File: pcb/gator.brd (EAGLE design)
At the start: 101.6 x 81.3 mm, 85 parts, among them J2 POWER_JACKPTH, X1 USB-A-S, Y1 12MHz

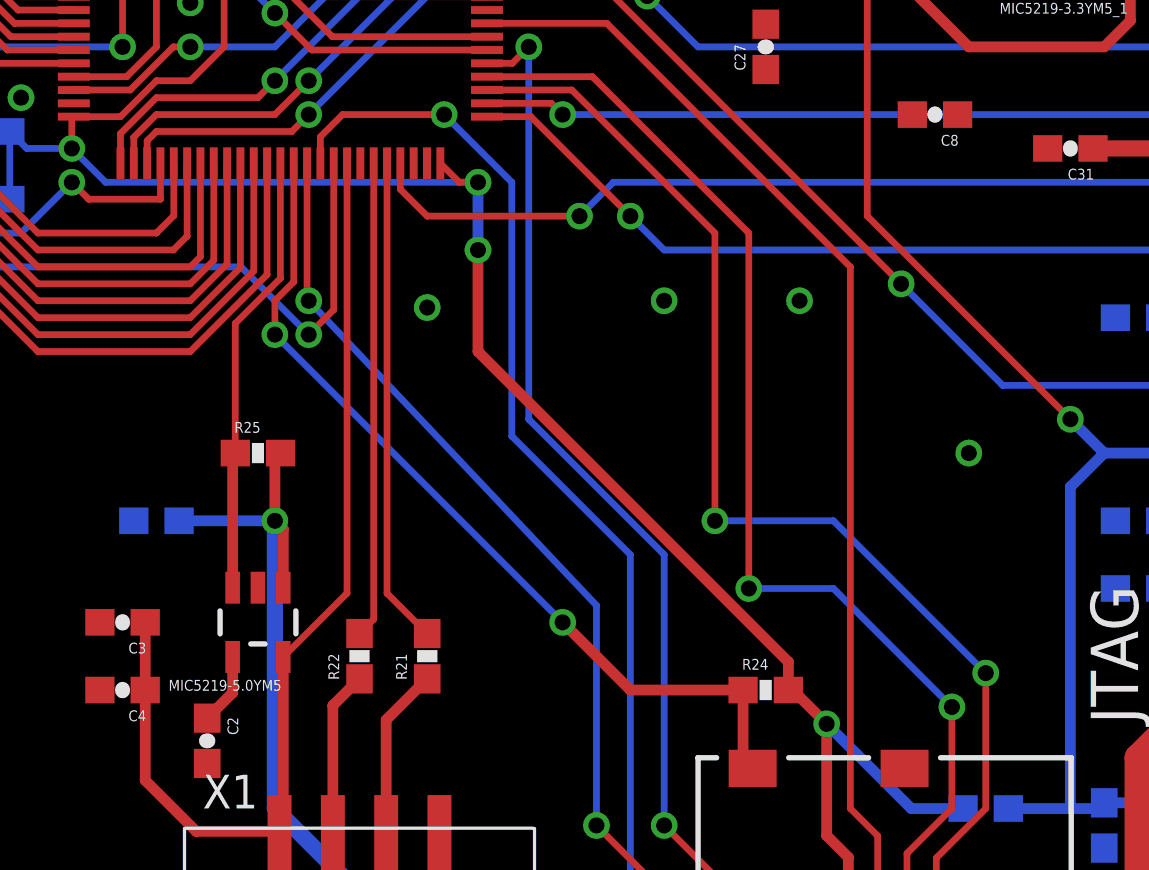
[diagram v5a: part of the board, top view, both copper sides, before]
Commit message: Minor cleanup; added signals for eyes; still need decoupling caps
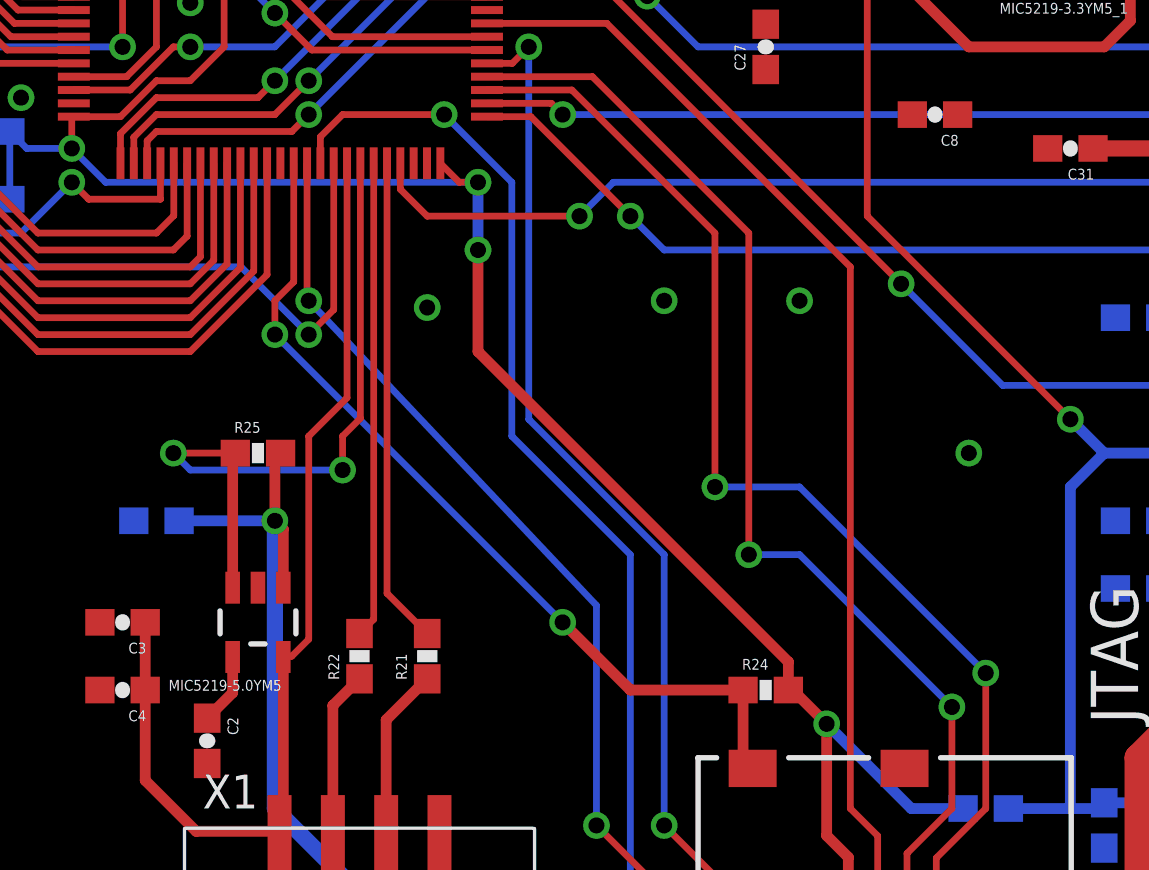
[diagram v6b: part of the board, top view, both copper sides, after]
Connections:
- new net LED_LEFT: FPGA.P100
- new net LED_RIGHT: U$1.63
- net USB_EN: now also U$1.69; no longer U$1.63
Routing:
- net USB_EN: track 16.7 -> 25.8 mm, vias 0 -> 2
- net SD_D3: track 48.0 -> 47.2 mm
- net SD_D2: track 48.7 -> 48.0 mm
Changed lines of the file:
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@@
 <wire x1="83.87" y1="12.75" x2="85.725" y2="14.605" width="0.254" layer="1"/>
 <wire x1="85.725" y1="14.605" x2="85.725" y2="19.685" width="0.254" layer="1"/>
-<via x="75.565" y="25.4" extent="1-16" drill="0.6"/>
-<wire x1="85.725" y1="19.685" x2="80.01" y2="25.4" width="0.254" layer="16"/>
-<wire x1="80.01" y1="25.4" x2="75.565" y2="25.4" width="0.254" layer="16"/>
+<via x="75.565" y="26.67" extent="1-16" drill="0.6"/>
+<wire x1="85.725" y1="19.685" x2="78.74" y2="26.67" width="0.254" layer="16"/>
+<wire x1="78.74" y1="26.67" x2="75.565" y2="26.67" width="0.254" layer="16"/>
 <wire x1="67.011971875" y1="41.561971875" x2="70.198028125" y2="41.561971875" width="0.254" layer="1"/>
 <wire x1="70.198028125" y1="41.561971875" x2="75.565" y2="36.195" width="0.254" layer="1"/>
-<wire x1="75.565" y1="36.195" x2="75.565" y2="25.4" width="0.254" layer="1"/>
+<wire x1="75.565" y1="36.195" x2="75.565" y2="26.67" width="0.254" layer="1"/>
 </signal>
 <signal name="SD_D3">
@@
 <wire x1="82.77" y1="12.92" x2="84.455" y2="14.605" width="0.254" layer="1"/>
 <wire x1="84.455" y1="14.605" x2="84.455" y2="18.415" width="0.254" layer="1"/>
-<via x="76.835" y="22.86" extent="1-16" drill="0.6"/>
-<wire x1="84.455" y1="18.415" x2="80.01" y2="22.86" width="0.254" layer="16"/>
-<wire x1="80.01" y1="22.86" x2="76.835" y2="22.86" width="0.254" layer="16"/>
+<via x="76.835" y="24.13" extent="1-16" drill="0.6"/>
+<wire x1="84.455" y1="18.415" x2="78.74" y2="24.13" width="0.254" layer="16"/>
+<wire x1="78.74" y1="24.13" x2="76.835" y2="24.13" width="0.254" layer="16"/>
 <wire x1="67.011971875" y1="42.061971875" x2="70.968028125" y2="42.061971875" width="0.254" layer="1"/>
 <wire x1="70.968028125" y1="42.061971875" x2="76.835" y2="36.195" width="0.254" layer="1"/>
-<wire x1="76.835" y1="36.195" x2="76.835" y2="22.86" width="0.254" layer="1"/>
+<wire x1="76.835" y1="36.195" x2="76.835" y2="24.13" width="0.254" layer="1"/>
 </signal>
 <signal name="SD_CLK">
@@
 <contactref element="C4" pad="1"/>
 <contactref element="U$1" pad="68"/>
-<wire x1="61.761971875" y1="22.681871875" x2="61.761971875" y2="38.811971875" width="0.254" layer="1"/>
-<wire x1="61.761971875" y1="22.681871875" x2="59.37" y2="20.2899" width="0.254" layer="1"/>
 <contactref element="X1" pad="VBUS"/>
 <wire x1="54.19" y1="21.59" x2="54.19" y2="19.05" width="0.4064" layer="1"/>
@@
 <wire x1="59.37" y1="20.2899" x2="59.37" y2="13.75" width="0.4064" layer="1"/>
 <wire x1="59.37" y1="13.75" x2="59.23" y2="13.61" width="0.4064" layer="1"/>
+<wire x1="59.37" y1="20.2899" x2="59.4001" y2="20.32" width="0.254" layer="1"/>
+<wire x1="59.4001" y1="20.32" x2="59.69" y2="20.32" width="0.254" layer="1"/>
+<wire x1="59.69" y1="20.32" x2="60.325" y2="20.955" width="0.254" layer="1"/>
+<wire x1="60.325" y1="20.955" x2="60.325" y2="28.575" width="0.254" layer="1"/>
+<wire x1="60.325" y1="28.575" x2="61.761971875" y2="30.011971875" width="0.254" layer="1"/>
+<wire x1="61.761971875" y1="30.011971875" x2="61.761971875" y2="38.811971875" width="0.254" layer="1"/>
 </signal>
 <signal name="N$4">
@@
 <signal name="USB_EN">
 <contactref element="MIC5219-5.0YM5" pad="3"/>
-<contactref element="U$1" pad="63"/>
-<wire x1="59.261971875" y1="34.496971875" x2="59.261971875" y2="38.811971875" width="0.254" layer="1"/>
 <contactref element="R25" pad="1"/>
 <wire x1="57.47" y1="22.8901" x2="57.47" y2="27.84" width="0.4064" layer="1"/>
 <wire x1="57.47" y1="27.84" x2="57.57" y2="27.94" width="0.4064" layer="1"/>
-<wire x1="57.57" y1="27.94" x2="57.57" y2="32.805" width="0.254" layer="1"/>
-<wire x1="57.57" y1="32.805" x2="59.261971875" y2="34.496971875" width="0.254" layer="1"/>
+<contactref element="U$1" pad="69"/>
+<via x="61.595" y="27.305" extent="1-16" drill="0.6"/>
+<wire x1="61.595" y1="27.305" x2="61.595" y2="28.575" width="0.254" layer="1"/>
+<wire x1="61.595" y1="28.575" x2="62.261971875" y2="29.241971875" width="0.254" layer="1"/>
+<wire x1="62.261971875" y1="29.241971875" x2="62.261971875" y2="38.811971875" width="0.254" layer="1"/>
+<via x="55.245" y="27.94" extent="1-16" drill="0.6"/>
+<wire x1="55.245" y1="27.94" x2="55.88" y2="27.305" width="0.254" layer="16"/>
+<wire x1="55.88" y1="27.305" x2="61.595" y2="27.305" width="0.254" layer="16"/>
+<wire x1="57.47" y1="27.84" x2="57.37" y2="27.94" width="0.254" layer="1"/>
+<wire x1="57.37" y1="27.94" x2="55.245" y2="27.94" width="0.254" layer="1"/>
 </signal>
 <signal name="VCCINT">
@@
 <wire x1="17.145" y1="53.34" x2="17.145" y2="57.59" width="0.254" layer="1"/>
 </signal>
+<signal name="LED_RIGHT">
+<contactref element="U$1" pad="63"/>
+</signal>
+<signal name="LED_LEFT">
+<contactref element="FPGA" pad="P100"/>
+</signal>
 </signals>

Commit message: Added gator and his eyeballs
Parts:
- added LED_L_EYE, LED_R_EYE: (no value), led:LED3MM
- added R36, R37: 120, SparkFun-Passives:0603-RES
- added U$4: GATOR_HEAD, gator:GATOR_HEAD
- moved C16 0.13 mm to (36.8, 63.6)
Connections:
- new net N$11: LED_L_EYE.A, R36.1
- new net N$12: LED_R_EYE.A, R37.1
- net GND: now also LED_L_EYE.K, LED_R_EYE.K, U$4.L, U$4.R
- net LED_LEFT: now also R36.2
- net LED_RIGHT: now also R37.2
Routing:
- net LED_LEFT: track 0.00 -> 43.1 mm, vias 0 -> 1
- net LED_RIGHT: track 0.00 -> 24.7 mm, vias 0 -> 1
- net N$12: track 0.00 -> 7.06 mm
- net N$11: track 0.00 -> 7.06 mm
- net USB_EN: track 25.8 -> 23.0 mm
- added copper zone on layer 16, net N$32
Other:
- board text added: "Jeff Theusch Rev A, Jan 2013"
- board text added: "{Gator Vision}"
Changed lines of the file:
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@@
 <board>
 <plain>
-<wire x1="0" y1="0" x2="0" y2="81.28" width="0.4064" layer="20"/>
-<wire x1="0" y1="81.28" x2="101.6" y2="81.28" width="0.4064" layer="20"/>
-<wire x1="101.6" y1="81.28" x2="101.6" y2="0" width="0.4064" layer="20"/>
-<wire x1="101.6" y1="0" x2="0" y2="0" width="0.4064" layer="20"/>
+<wire x1="0" y1="0" x2="0" y2="81.28" width="0" layer="20"/>
+<wire x1="0" y1="81.28" x2="101.6" y2="81.28" width="0" layer="20"/>
+<wire x1="101.6" y1="81.28" x2="101.6" y2="0" width="0" layer="20"/>
+<wire x1="101.6" y1="0" x2="0" y2="0" width="0" layer="20"/>
 <hole x="2.54" y="2.54" drill="2.8"/>
 <hole x="2.54" y="78.74" drill="2.8"/>
 <hole x="99.06" y="78.74" drill="2.8"/>
 <hole x="99.06" y="2.54" drill="2.8"/>
+<text x="51.435" y="3.81" size="1.778" layer="16" font="vector" ratio="17" rot="MR0">Jeff Theusch
+Rev A, Jan 2013</text>
+<text x="40.005" y="26.67" size="1.4224" layer="1" font="vector" ratio="15">{Gator Vision}</text>
 </plain>
 <attributes>
@@
 <element name="NCP565ST12T3G" library="microbuilder" package="SOT223-R" value="" x="41.91" y="72.39" rot="R90"/>
 <element name="C15" library="SparkFun-Passives" package="0603-CAP" value="100n" x="36.195" y="70.485" rot="R90"/>
-<element name="C16" library="SparkFun-Passives" package="0603-CAP" value="2.2u" x="36.83" y="63.5"/>
+<element name="C16" library="SparkFun-Passives" package="0603-CAP" value="2.2u" x="36.83" y="63.627"/>
 <element name="C17" library="SparkFun-Passives" package="0603-CAP" value="100n" x="26.67" y="36.83" rot="MR0"/>
 <element name="U$1" library="gator" package="LQFP-100" value="STM32F417VGT6" x="66.411971875" y="53.711971875" rot="R180"/>
@@
 <element name="R34" library="SparkFun-Passives" package="0603-RES" value="10K" x="21.59" y="64.135"/>
 <element name="R35" library="SparkFun-Passives" package="0603-RES" value="10K" x="21.59" y="62.23"/>
+<element name="LED_L_EYE" library="led" package="LED3MM" value="" x="41.275" y="12.192" smashed="yes" rot="R90">
+<attribute name="VALUE" x="42.925996875" y="14.097" size="1.27" layer="27" ratio="10" rot="R90"/>
+</element>
+<element name="LED_R_EYE" library="led" package="LED3MM" value="" x="45.72" y="12.192" smashed="yes" rot="R90">
+<attribute name="VALUE" x="47.371003125" y="14.096996875" size="1.27" layer="27" ratio="10" rot="R90"/>
+</element>
+<element name="R36" library="SparkFun-Passives" package="0603-RES" value="120" x="38.735" y="17.78" rot="MR90"/>
+<element name="R37" library="SparkFun-Passives" package="0603-RES" value="120" x="48.26" y="17.78" rot="MR90"/>
+<element name="U$4" library="gator" package="GATOR_HEAD" value="GATOR_HEAD" x="33.274" y="2.54"/>
 </elements>
 <signals>
@@
 <via x="45.72" y="44.196" extent="1-16" drill="0.6"/>
 <via x="64.77" y="33.401" extent="1-16" drill="0.6"/>
-<via x="55.88" y="44.831" extent="1-16" drill="0.6"/>
 <via x="72.39" y="4.191" extent="1-16" drill="0.6"/>
 <via x="34.29" y="61.341" extent="1-16" drill="0.6"/>
@@
 <via x="25.4" y="58.801" extent="1-16" drill="0.6"/>
 <via x="54.61" y="52.705" extent="1-16" drill="0.6"/>
+<contactref element="LED_L_EYE" pad="K"/>
+<contactref element="LED_R_EYE" pad="K"/>
+<via x="49.53" y="9.906" extent="1-16" drill="0.6"/>
+<via x="37.465" y="9.906" extent="1-16" drill="0.6"/>
+<contactref element="U$4" pad="L"/>
+<contactref element="U$4" pad="R"/>
+<wire x1="30.384071875" y1="56.44801875" x2="27.884071875" y2="56.44801875" width="0" layer="19" extent="1-1"/>
 </signal>
 <signal name="/TRST">
@@
 <wire x1="61.595" y1="28.575" x2="62.261971875" y2="29.241971875" width="0.254" layer="1"/>
 <wire x1="62.261971875" y1="29.241971875" x2="62.261971875" y2="38.811971875" width="0.254" layer="1"/>
-<via x="55.245" y="27.94" extent="1-16" drill="0.6"/>
-<wire x1="55.245" y1="27.94" x2="55.88" y2="27.305" width="0.254" layer="16"/>
-<wire x1="55.88" y1="27.305" x2="61.595" y2="27.305" width="0.254" layer="16"/>
+<via x="57.785" y="29.21" extent="1-16" drill="0.6"/>
 <wire x1="57.47" y1="27.84" x2="57.37" y2="27.94" width="0.254" layer="1"/>
-<wire x1="57.37" y1="27.94" x2="55.245" y2="27.94" width="0.254" layer="1"/>
+<wire x1="57.785" y1="29.21" x2="59.69" y2="27.305" width="0.254" layer="16"/>
+<wire x1="59.69" y1="27.305" x2="61.595" y2="27.305" width="0.254" layer="16"/>
+<wire x1="57.57" y1="27.94" x2="57.785" y2="28.155" width="0.254" layer="1"/>
+<wire x1="57.785" y1="28.155" x2="57.785" y2="29.21" width="0.254" layer="1"/>
 </signal>
 <signal name="VCCINT">
@@
 <via x="28.575" y="58.42" extent="1-16" drill="0.6"/>
 <wire x1="28.575" y1="59.055" x2="28.575" y2="58.42" width="0.6096" layer="1"/>
-<wire x1="28.575" y1="59.055" x2="39.37" y2="69.85" width="0.6096" layer="1"/>
-<wire x1="39.37" y1="69.85" x2="40.64" y2="69.85" width="0.6096" layer="1"/>
-<wire x1="40.64" y1="69.85" x2="43.18" y2="72.39" width="0.6096" layer="1"/>
+<wire x1="28.575" y1="59.055" x2="35.56" y2="66.04" width="0.6096" layer="1"/>
+<wire x1="35.56" y1="66.04" x2="36.83" y2="66.04" width="0.6096" layer="1"/>
+<wire x1="36.83" y1="66.04" x2="43.18" y2="72.39" width="0.6096" layer="1"/>
 <wire x1="43.18" y1="72.39" x2="44.96" y2="72.39" width="0.6096" layer="1"/>
 <wire x1="28.575" y1="58.42" x2="31.75" y2="58.42" width="0.6096" layer="16"/>
-<wire x1="31.75" y1="58.42" x2="35.98" y2="63.5" width="0" layer="19" extent="1-1"/>
+<wire x1="35.56" y1="66.04" x2="35.98" y2="63.627" width="0" layer="19" extent="1-1"/>
 </signal>
 <signal name="N$3">
@@
 <signal name="LED_RIGHT">
 <contactref element="U$1" pad="63"/>
+<contactref element="R37" pad="2"/>
+<wire x1="59.261971875" y1="38.811971875" x2="59.261971875" y2="34.496971875" width="0.254" layer="1"/>
+<wire x1="59.261971875" y1="34.496971875" x2="57.785" y2="33.02" width="0.254" layer="1"/>
+<via x="57.785" y="32.385" extent="1-16" drill="0.6"/>
+<wire x1="57.785" y1="33.02" x2="57.785" y2="32.385" width="0.254" layer="1"/>
+<wire x1="57.785" y1="32.385" x2="48.26" y2="22.86" width="0.254" layer="16"/>
+<wire x1="48.26" y1="22.86" x2="48.26" y2="18.63" width="0.254" layer="16"/>
 </signal>
 <signal name="LED_LEFT">
 <contactref element="FPGA" pad="P100"/>
+<contactref element="R36" pad="2"/>
+<via x="26.035" y="50.8" extent="1-16" drill="0.6"/>
+<wire x1="25.884071875" y1="56.44801875" x2="25.884071875" y2="50.950928125" width="0.254" layer="1"/>
+<wire x1="25.884071875" y1="50.950928125" x2="26.035" y2="50.8" width="0.254" layer="1"/>
+<wire x1="26.035" y1="50.8" x2="26.035" y2="50.165" width="0.254" layer="16"/>
+<wire x1="26.035" y1="50.165" x2="38.735" y2="37.465" width="0.254" layer="16"/>
+<wire x1="38.735" y1="37.465" x2="38.735" y2="18.63" width="0.254" layer="16"/>
+</signal>
+<signal name="N$11">
+<contactref element="R36" pad="1"/>
+<contactref element="LED_L_EYE" pad="A"/>
+<wire x1="38.735" y1="16.93" x2="38.735" y2="13.462" width="0.254" layer="16"/>
+<wire x1="38.735" y1="13.462" x2="41.275" y2="10.922" width="0.254" layer="16"/>
+</signal>
+<signal name="N$12">
+<contactref element="R37" pad="1"/>
+<contactref element="LED_R_EYE" pad="A"/>
+<wire x1="48.26" y1="16.93" x2="48.26" y2="13.462" width="0.254" layer="16"/>
+<wire x1="48.26" y1="13.462" x2="45.72" y2="10.922" width="0.254" layer="16"/>
+</signal>
+<signal name="N$32">
+<polygon width="0" layer="16" pour="cutout">
+<vertex x="25.4" y="2.54"/>
+<vertex x="25.4" y="8.89"/>
+<vertex x="53.975" y="8.89"/>
+<vertex x="53.975" y="2.54"/>
+</polygon>
 </signal>
 </signals>
 </board>
 </drawing>
+<compatibility>
+<note version="6.3" minversion="6.2.2" severity="warning">
+Since Version 6.2.2 text objects can contain more than one line,
+which will not be processed correctly with this version.
+</note>
+</compatibility>
 </eagle>

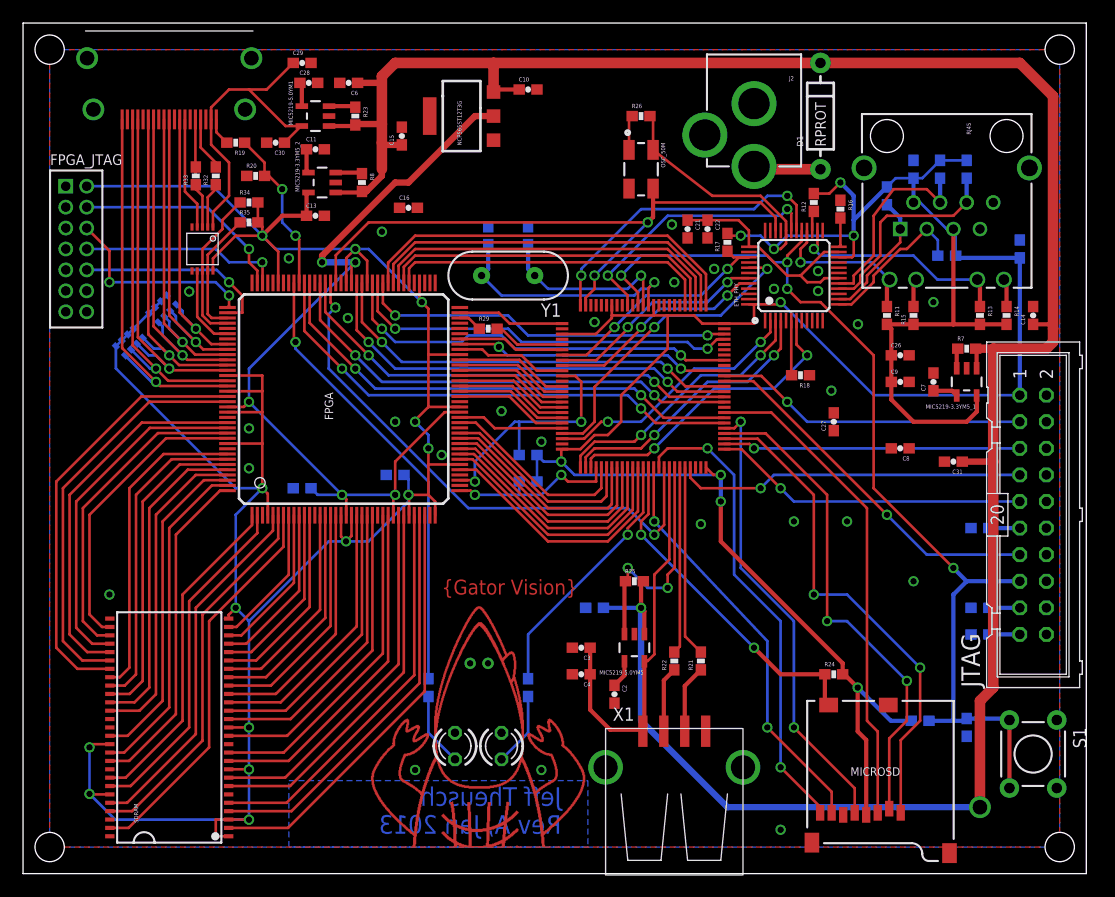
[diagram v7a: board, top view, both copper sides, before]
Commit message: Solved all ERC warnings and connected all airwires
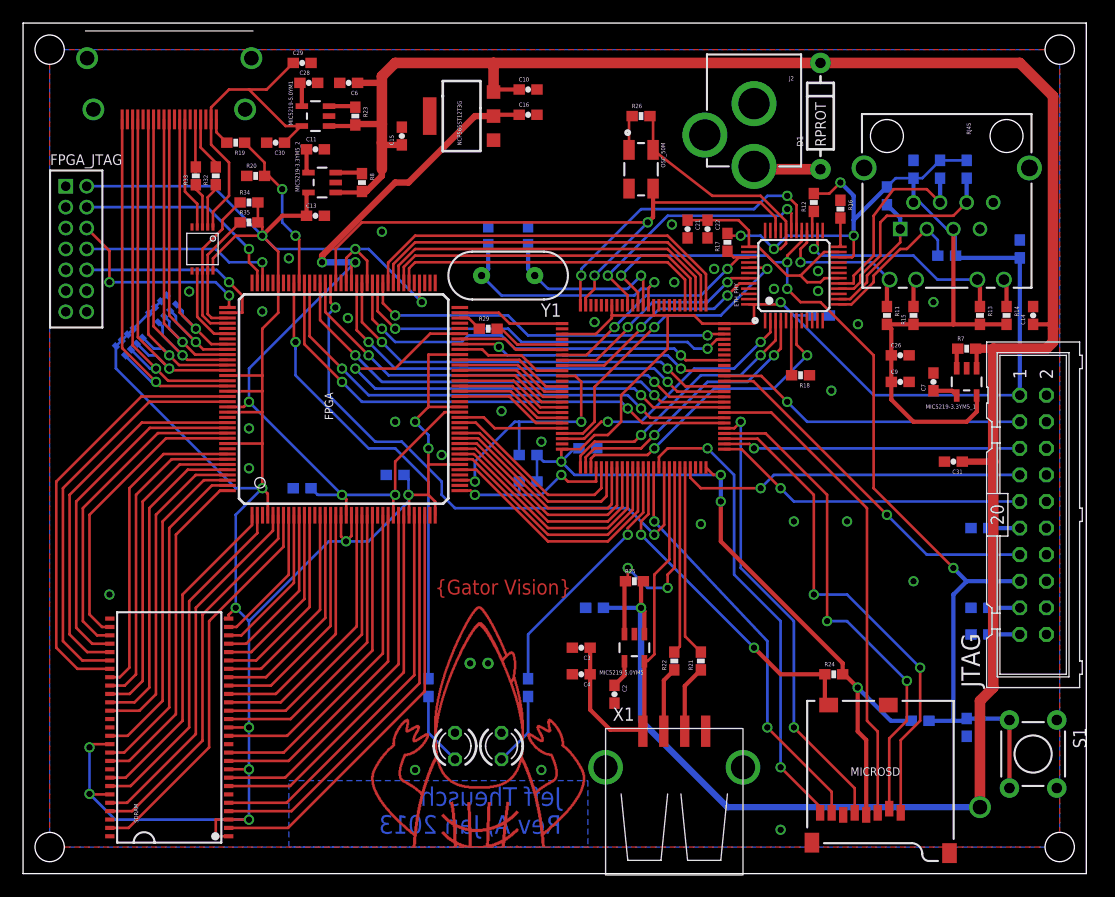
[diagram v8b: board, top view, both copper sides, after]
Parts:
- JTAG: value (none) -> HEADER
- LED_L_EYE, LED_R_EYE: value (none) -> GRN
- NCP565ST12T3G: value (none) -> 1.2V
- S1: value (none) -> 0
- moved C27 23.6 mm to (54.0, 40.6), flipped to the bottom, turned to 180 degrees
- moved C8 14.8 mm to (76.2, 53.3), flipped to the bottom
- moved C16 14.5 mm to (48.3, 72.5)
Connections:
- removed net DDC_EN: U$3.6
- removed net RMII_REF_CLK: ETH_PHY.25
- removed net VBAT: U$1.6
- removed net VCAP_1: U$1.49
- removed net VCAP_2: U$1.73
- removed net VDDA: U$1.22
- removed net VREFP: U$1.21
- net FSMC_CLK: now also FPGA.P67
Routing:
- net FSMC_CLK: track 0.00 -> 48.2 mm, vias 0 -> 2
- net VCCIO: track 255.6 -> 259.8 mm
- net +3V3: track 268.8 -> 272.8 mm
- net VCCINT: track 84.0 -> 86.5 mm
- net FPGA_CLK1: track 53.1 -> 55.4 mm
- net LED_LEFT: track 43.1 -> 45.3 mm
- net D3: track 47.2 -> 47.9 mm
- net D2: track 48.4 -> 49.1 mm
